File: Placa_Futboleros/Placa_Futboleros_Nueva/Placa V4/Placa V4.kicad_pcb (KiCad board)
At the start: 2 copper layers, 52 x 100 mm, 23 parts, among them J1 BAT, J2 Motor_Izq_Adelante, J3 Motor_Izq_Atras, J4 Motor_Der_Adelante, J5 Motor_Der_Atras, U1 ESP32-DEVKIT-V1, U2 DRV8833, U3 DRV8833, U5 ACS712xLCTR-30A

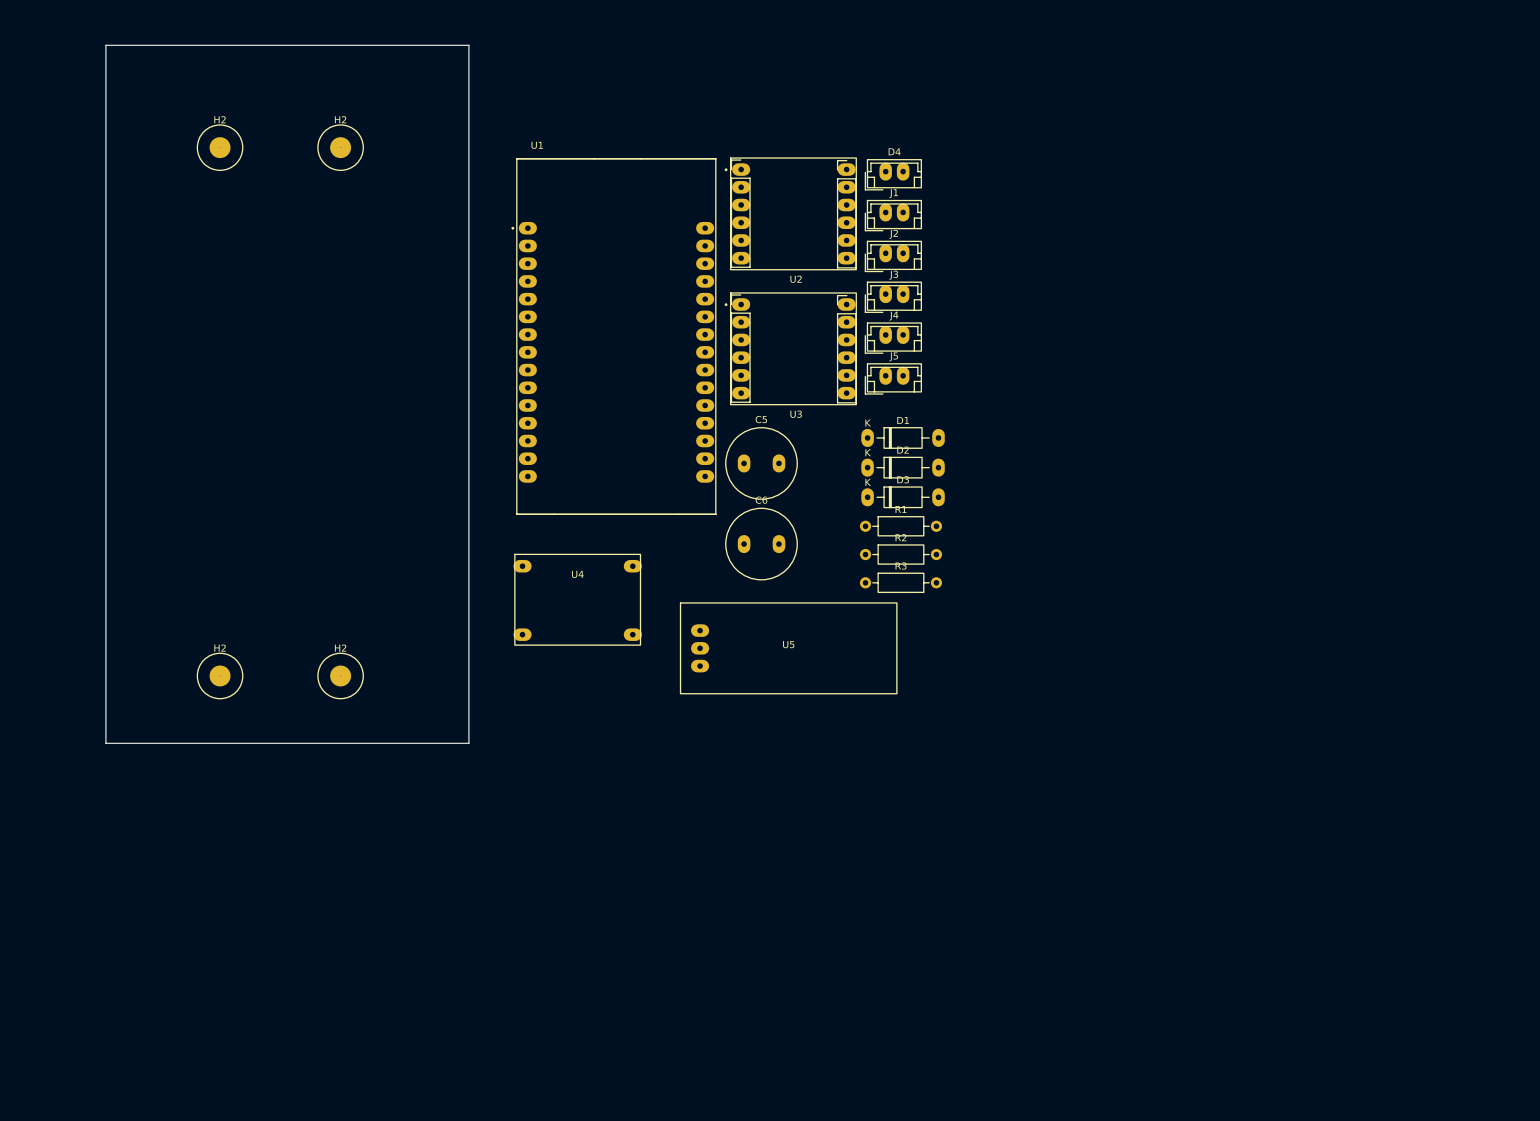
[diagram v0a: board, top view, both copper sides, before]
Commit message: Idea Placa V4 Futboleros
Se diseña un primer sketch de la placa v4 de los futboleros
en kicad, la misma contiene todas las mejoras circuitales,
y pasa a ser un poco mas grande 125mmx60mm (antes 100mmx52mm).
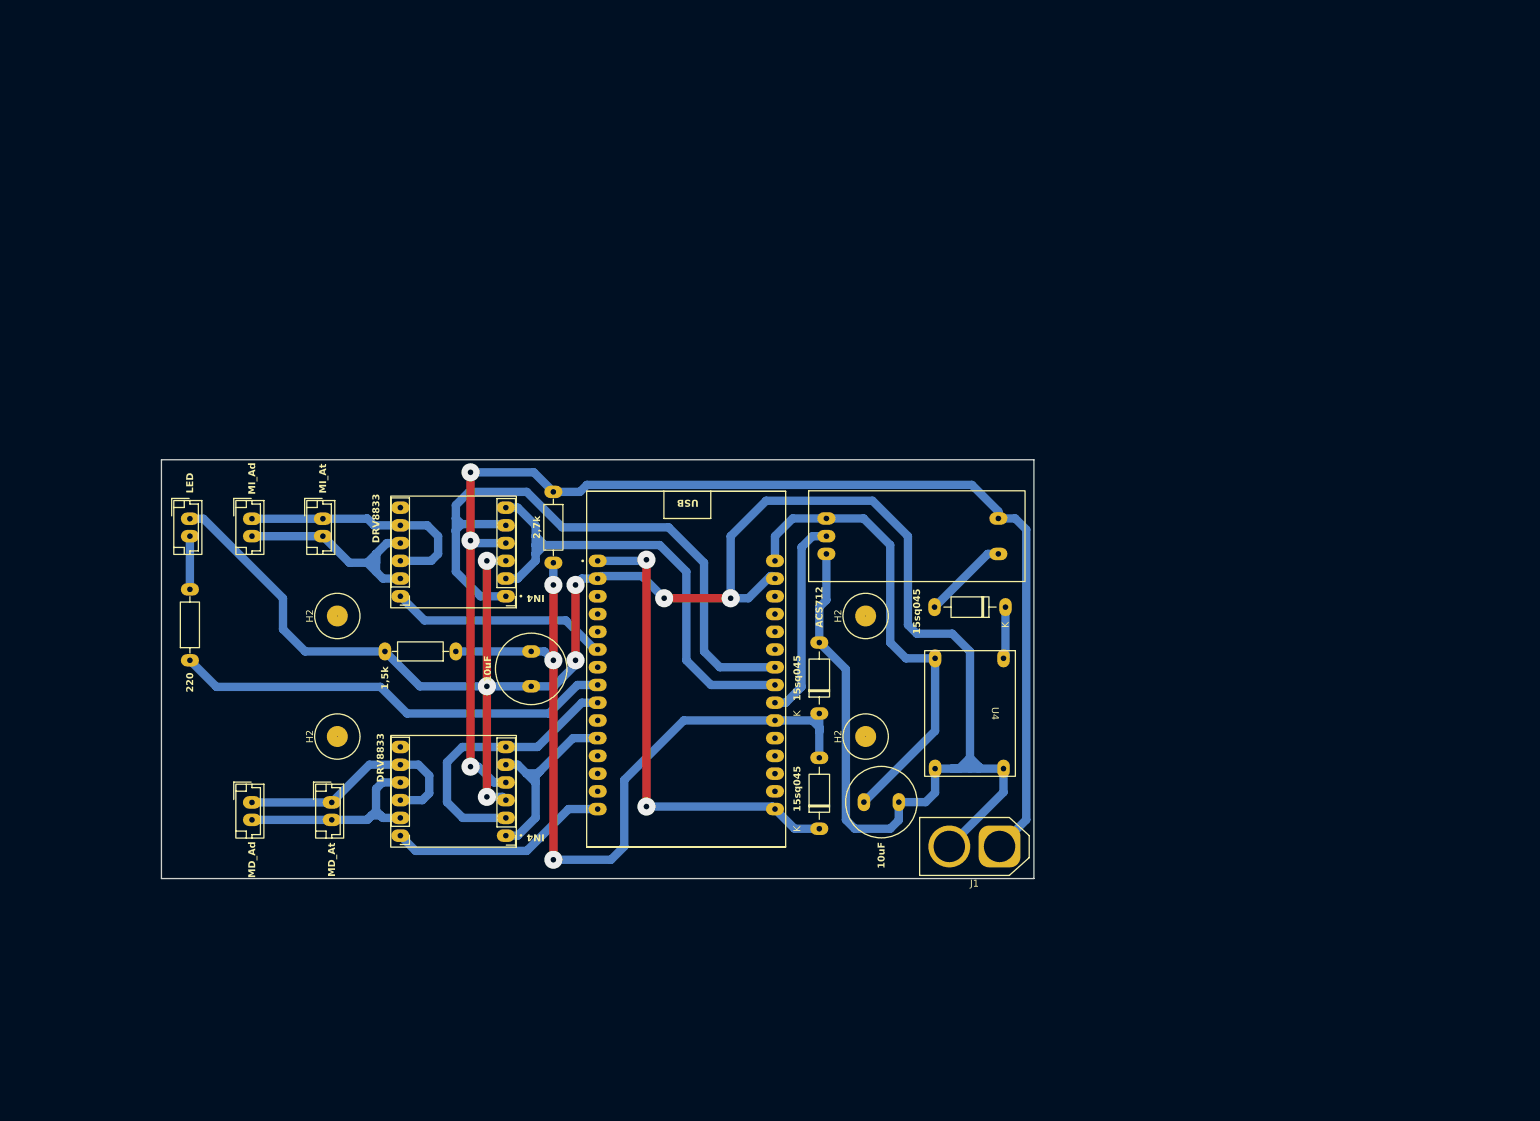
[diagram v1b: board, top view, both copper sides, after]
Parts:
- D4: value LED_RED -> LED
- J1: footprint Connector_JST:JST_EH_B2B-EH-A_1x02_P2.50mm_Vertical -> Connector_AMASS:AMASS_XT60-F_1x02_P7.20mm_Vertical
- J2: value Motor_Izq_Adelante -> MI_Ad
- J3: value Motor_Izq_Atras -> MI_At
- J4: value Motor_Der_Adelante -> MD_Ad
- J5: value Motor_Der_Atras -> MD_At
- U1: value ESP32-DEVKIT-V1 -> ESP-30p
- U5: value ACS712xLCTR-30A -> ACS712
- moved J4 112.8 mm to (73.6, 136.7), turned to -90 degrees
- moved D4 111.4 mm to (64.7, 96.1), turned to -90 degrees
- moved J5 100.2 mm to (85.0, 136.7), turned to -90 degrees
- moved R1 98.7 mm to (64.7, 116.3), turned to 90 degrees
- moved J2 98.4 mm to (73.6, 96.1), turned to -90 degrees
- moved H2 92.9 mm to (161.5, 127.3), turned to 90 degrees
- moved J1 92.3 mm to (180.7, 143.0), turned to 180 degrees
- moved J3 86.8 mm to (83.7, 96.1), turned to -90 degrees
- moved H2 86.0 mm to (85.8, 127.3), turned to 90 degrees
- moved H2 75.7 mm to (161.5, 110.0), turned to 90 degrees
- moved H2 67.1 mm to (85.8, 110.0), turned to 90 degrees
- moved U3 65.9 mm to (102.1, 125.2), turned to 180 degrees
- moved R3 59.5 mm to (102.8, 115.1), turned to 180 degrees
- moved U4 58.5 mm to (176.4, 124.0), turned to -90 degrees
- moved U2 57.1 mm to (102.1, 90.9), turned to 180 degrees
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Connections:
- U1 pad 2: unconnected-(U1-GND-Pad2) -> GND
- U1 pad 28: LED_Encendido -> unconnected-(U1-D13-Pad28)
- U1 pad 8: unconnected-(U1-D5-Pad8) -> LED_Encendido
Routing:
- net GND: track 0.00 -> 320.2 mm, vias 0 -> 7
- net VCC: track 0.00 -> 184.8 mm, vias 0 -> 3
- net /ADC: track 0.00 -> 117.7 mm, vias 0 -> 3
- net IN_M1A: track 0.00 -> 91.5 mm
- net IN_M1B: track 0.00 -> 69.3 mm
- net 5V: track 0.00 -> 68.8 mm
- net 3V3: track 0.00 -> 68.5 mm, vias 0 -> 2
- net LED_Encendido: track 0.00 -> 63.3 mm
- net IN_M2B: track 0.00 -> 40.2 mm
- net Net-(J2-Pin_1): track 0.00 -> 36.1 mm
- net Net-(J4-Pin_1): track 0.00 -> 35.4 mm
- net Net-(J2-Pin_2): track 0.00 -> 34.8 mm
- net Net-(J4-Pin_2): track 0.00 -> 31.9 mm
- net SLEEP_M2: track 0.00 -> 31.7 mm
- net SLEEP_M1: track 0.00 -> 31.4 mm
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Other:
- board size 52 x 100 mm -> 125 x 60 mm
- board text added: "15sq045"
- board text added: "DRV8833"
- board text added: "IN4"

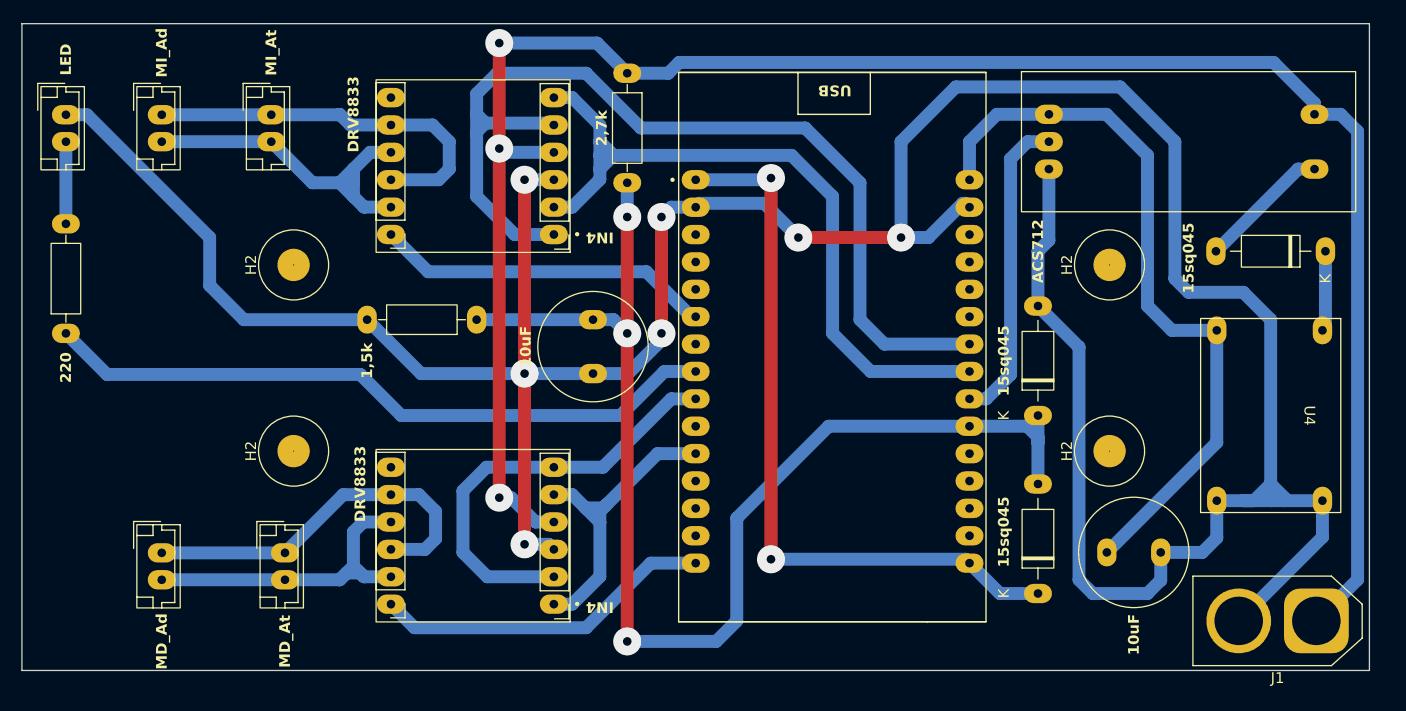
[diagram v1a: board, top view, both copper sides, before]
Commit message: Solcuión momentánea de ancho de pistas por 7A aprox
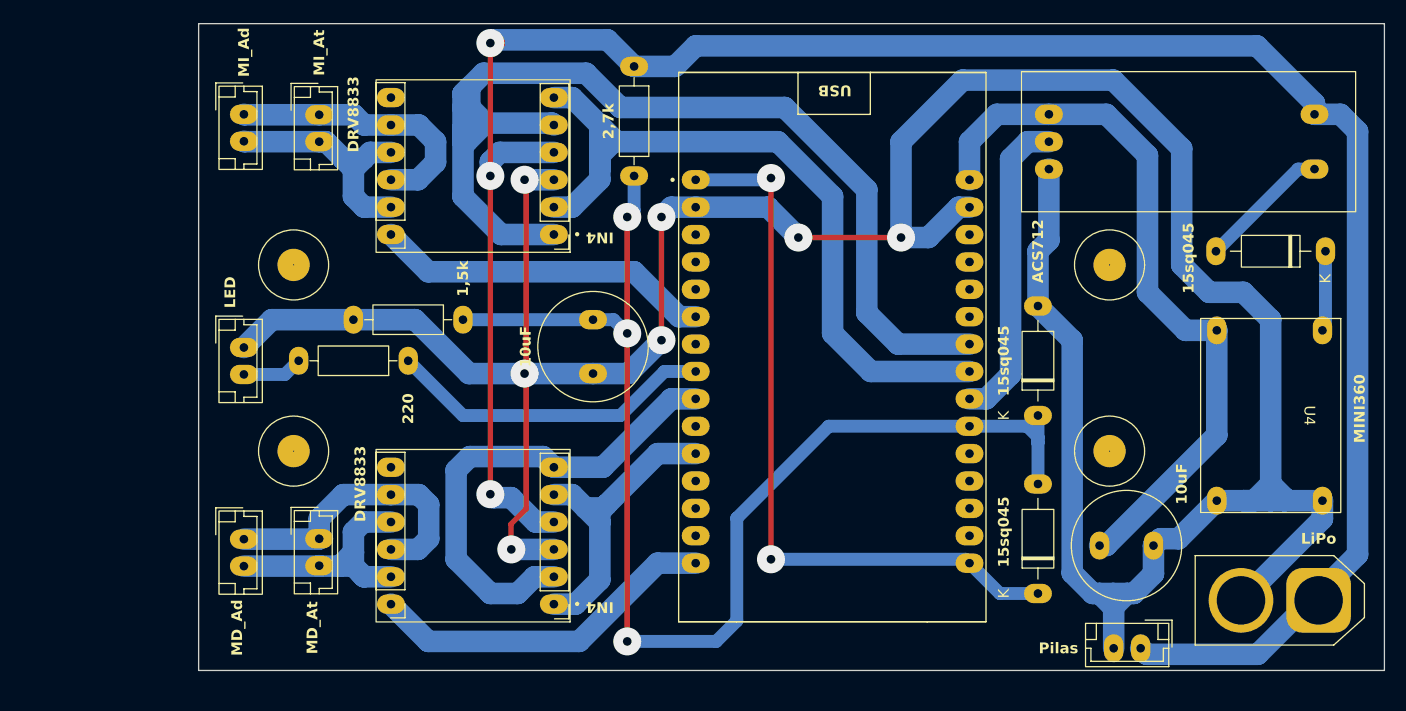
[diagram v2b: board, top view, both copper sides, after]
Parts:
- added J6: Pilas, Connector_JST:JST_EH_B2B-EH-A_1x02_P2.50mm_Vertical, F.Cu at (164.4, 145.5)
- J1: value BAT -> LiPo
- U1: value ESP-30p -> ESP32_30p
- moved R1 31.9 mm to (96.4, 118.9), turned to 180 degrees
- moved D4 27.2 mm to (81.2, 117.6)
- moved J4 7.73 mm to (81.2, 135.4)
- moved J2 7.62 mm to (81.2, 96.0)
- moved J3 4.45 mm to (88.2, 96.1)
- moved J5 3.43 mm to (88.2, 135.4)
- moved J1 1.92 mm to (180.9, 141.1)
- moved R3 1.27 mm to (101.5, 115.1)
- moved C5 0.93 mm to (160.6, 136.0)
- moved R2 0.90 mm to (117.4, 91.6)
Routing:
- net LED_Encendido: track 63.3 -> 30.5 mm
- net VCC: track 184.8 -> 207.0 mm
- net GND: track 320.2 -> 300.7 mm
- net Net-(J2-Pin_2): track 34.8 -> 23.7 mm
- net IN_M1A: track 91.5 -> 102.4 mm
- net Net-(J2-Pin_1): track 36.1 -> 25.5 mm
- net Net-(J4-Pin_2): track 31.9 -> 23.4 mm
- net Net-(J4-Pin_1): track 35.4 -> 27.4 mm
- net IN_M1B: track 69.3 -> 77.0 mm
- net IN_M2B: track 40.2 -> 45.1 mm
- net /ADC: track 117.7 -> 119.9 mm
- net Net-(D4-A): track 7.62 -> 5.61 mm
- net SLEEP_M2: track 31.7 -> 32.7 mm
- net 5V: track 68.8 -> 68.1 mm
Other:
- board size 125 x 60 mm -> 110 x 60 mm
- board text added: "MINI360"

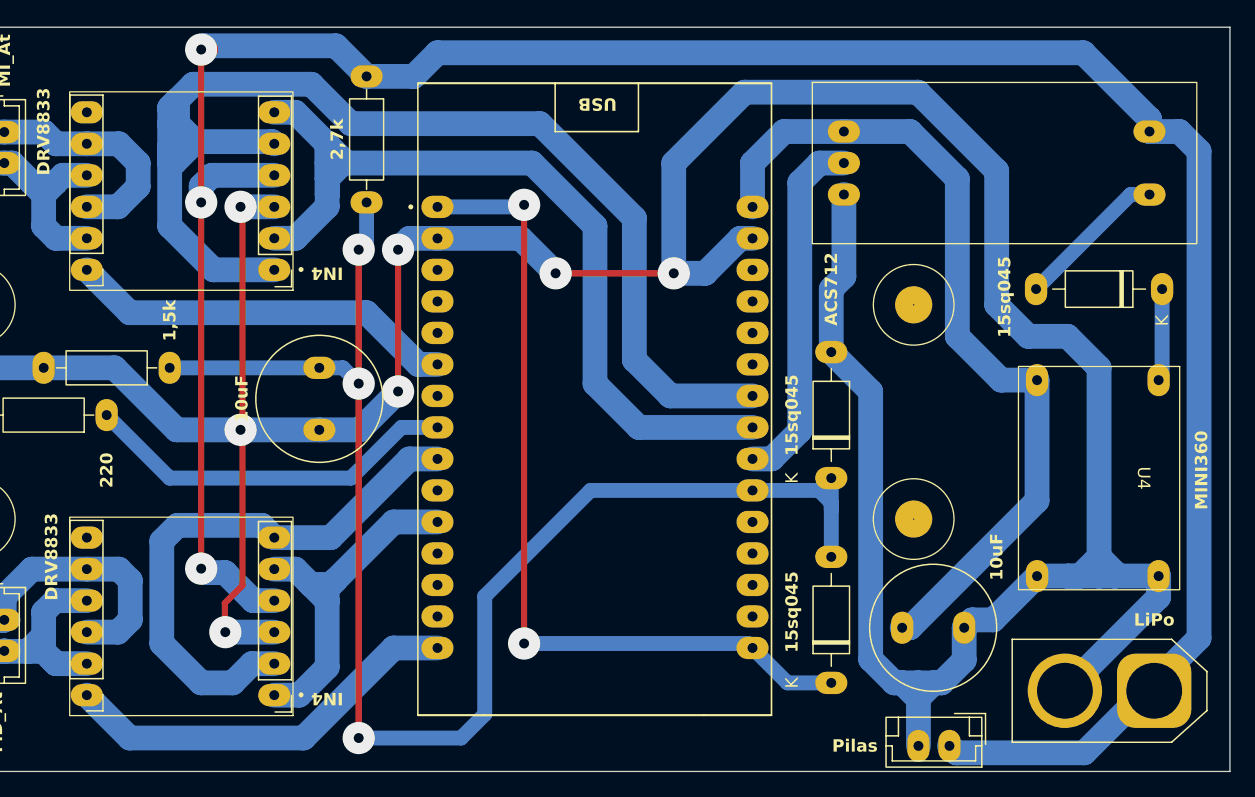
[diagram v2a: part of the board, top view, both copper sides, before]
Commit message: Actualización de Placa
Se actualiza la placa V4 para ancho de pistas, y
corrección de vías debajo de componentes
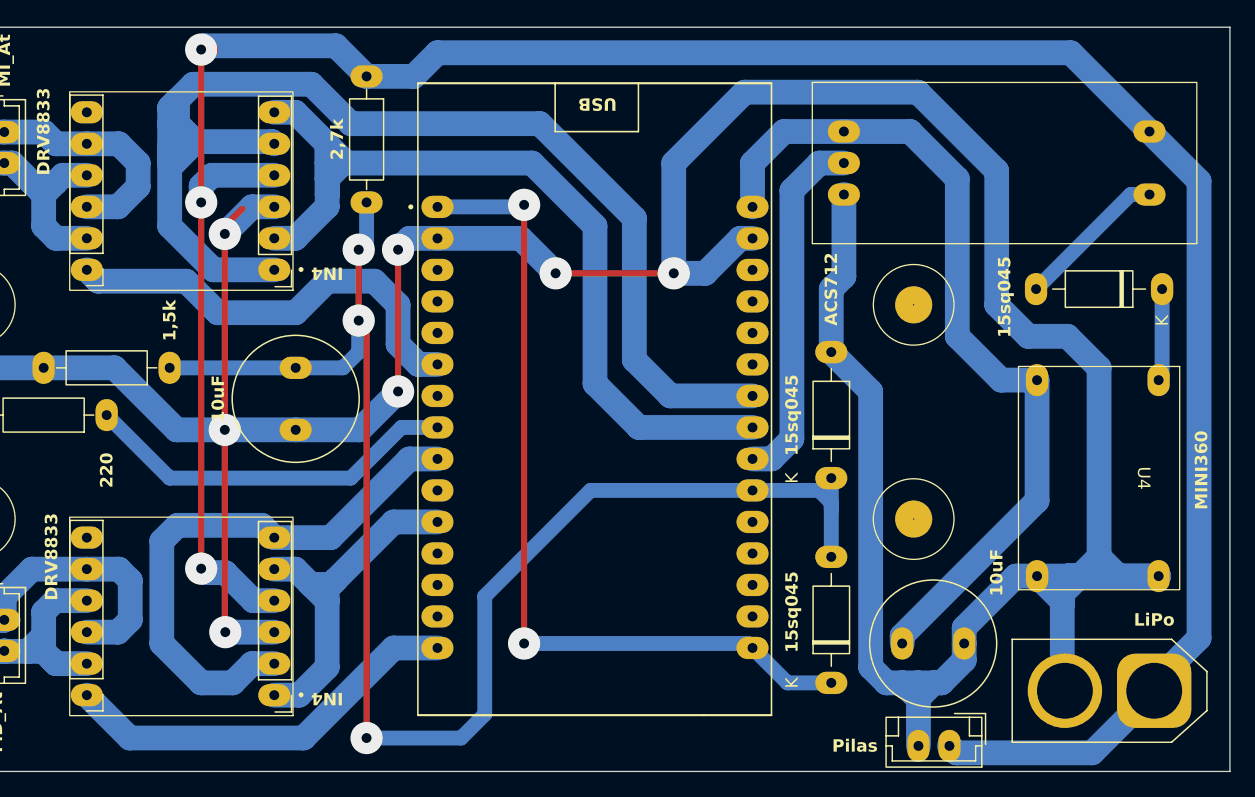
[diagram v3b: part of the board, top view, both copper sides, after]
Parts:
- moved C6 1.90 mm to (111.7, 115.1)
- moved C5 1.27 mm to (160.6, 137.3)
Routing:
- net GND: track 300.7 -> 313.3 mm
- net SLEEP_M1: track 31.4 -> 35.4 mm
- net /ADC: track 119.9 -> 122.0 mm
- net VCC: track 207.0 -> 204.9 mm
- net 5V: track 68.1 -> 69.0 mm
